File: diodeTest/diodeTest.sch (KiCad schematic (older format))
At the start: 3 parts

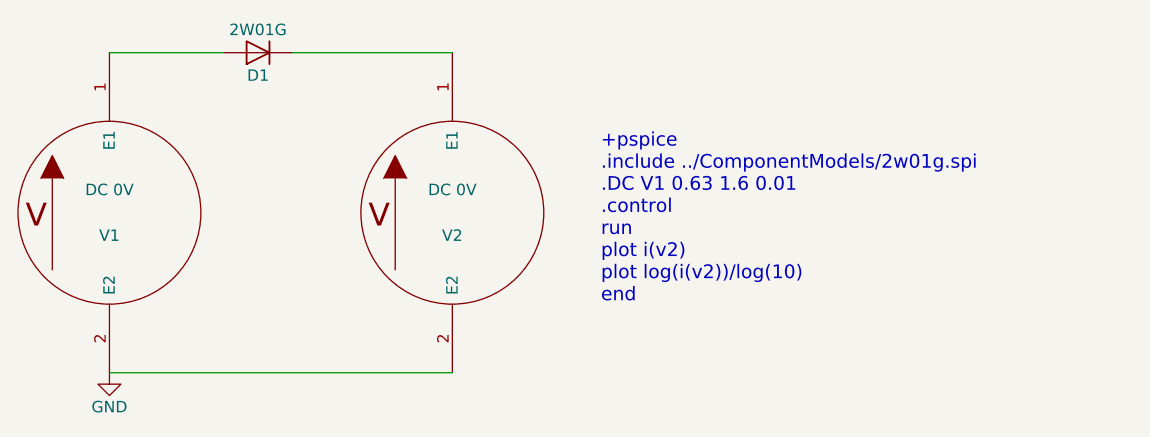
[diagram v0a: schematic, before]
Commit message: added bridge rectifier GBJ1506
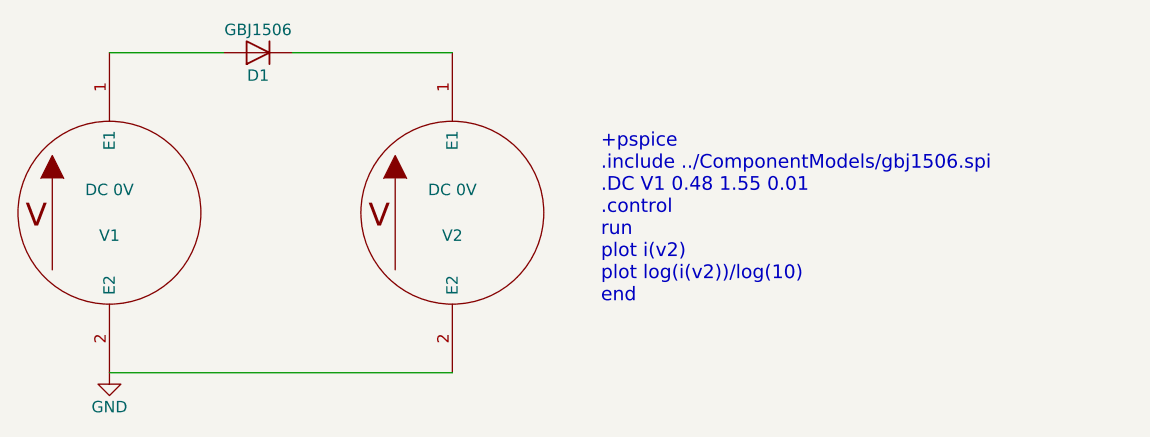
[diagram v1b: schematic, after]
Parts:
- D1: value 2W01G -> GBJ1506
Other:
- note added: "+pspice\n.include ../ComponentModels/gbj1506.spi\n.DC V1 0.48 1.55 0.01 \n.control\nrun\nplot i(v2)\nplot log(i(v2))/log(10)\nend"
- note removed: "+pspice\n.include ../ComponentModels/2w01g.spi\n.DC V1 0.63 1.6 0.01 \n.control\nrun\nplot i(v2)\nplot log(i(v2))/log(10)\nend"
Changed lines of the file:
@@
 LIBS:contrib
 LIBS:valves
-LIBS:mains-cache
+LIBS:diodeTest-cache
 EELAYER 25 0
 EELAYER END
@@
 $EndComp
 Text Notes 3050 1850 0    60   ~ 0
-+pspice\n.include ../ComponentModels/2w01g.spi\n.DC V1 0.63 1.6 0.01 \n.control\nrun\nplot i(v2)\nplot log(i(v2))/log(10)\nend
++pspice\n.include ../ComponentModels/gbj1506.spi\n.DC V1 0.48 1.55 0.01 \n.control\nrun\nplot i(v2)\nplot log(i(v2))/log(10)\nend
 $Comp
 L GND #PWR01
@@
 P 1550 750
 F 0 "D1" H 1550 850 50  0000 C CNN
-F 1 "2W01G" H 1550 650 50  0000 C CNN
+F 1 "GBJ1506" H 1550 650 50  0000 C CNN
 F 2 "" H 1550 750 50  0001 C CNN
 F 3 "" H 1550 750 50  0001 C CNN
